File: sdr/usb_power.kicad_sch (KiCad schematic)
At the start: 9 parts, among them J1 USB_C_Receptacle_USB2.0, U1 AMS1117-3.3

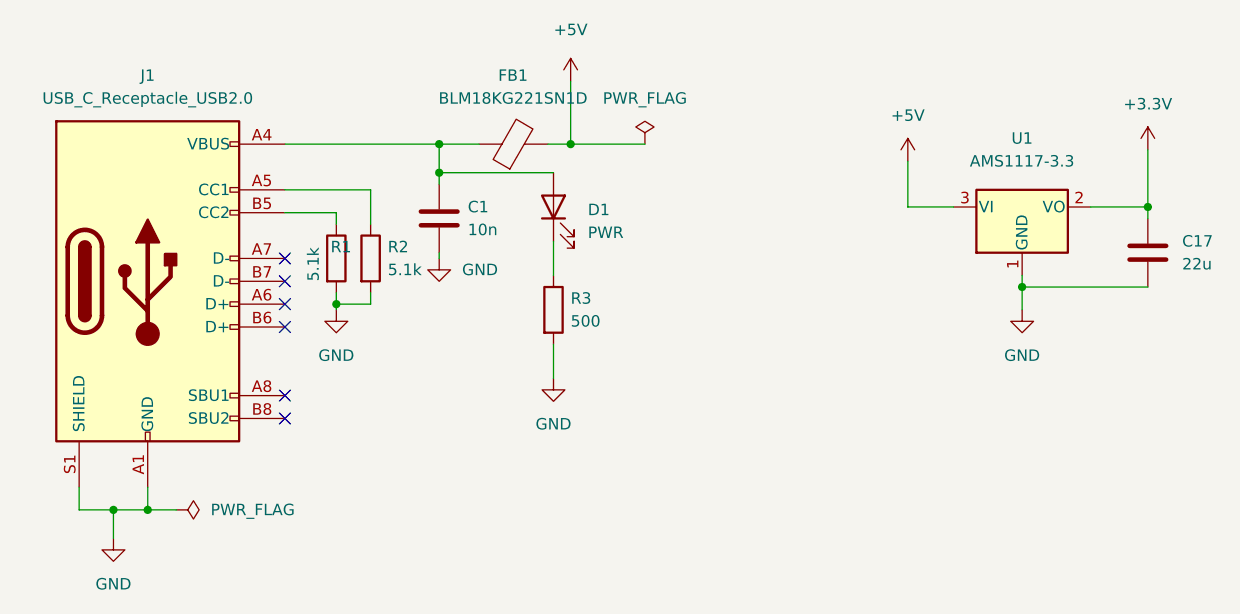
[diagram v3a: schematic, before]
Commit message: Tighten up design layout.
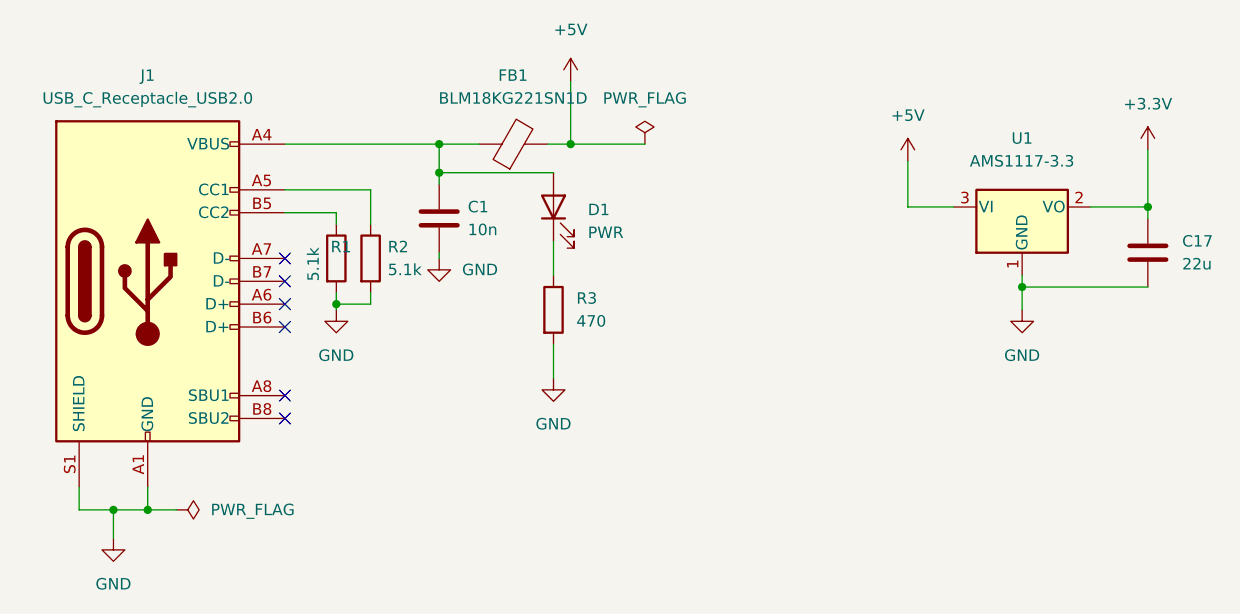
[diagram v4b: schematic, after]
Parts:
- C1: footprint Capacitor_SMD:C_0603_1608Metric -> Capacitor_SMD:C_0402_1005Metric
- R3: value 500 -> 470
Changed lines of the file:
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@@
   (symbol (lib_id "Device:R") (at 168.91 90.17 0) (unit 1)
     (in_bom yes) (on_board yes) (fields_autoplaced)
-    (property "Reference" "R3" (id 0) (at 170.815 88.8999 0)
-      (effects (font (size 1.27 1.27)) (justify left))
-    )
-    (property "Value" "500" (id 1) (at 170.815 91.4399 0)
+    (property "Reference" "R3" (id 0) (at 171.45 88.8999 0)
+      (effects (font (size 1.27 1.27)) (justify left))
+    )
+    (property "Value" "470" (id 1) (at 171.45 91.4399 0)
       (effects (font (size 1.27 1.27)) (justify left))
     )
@@
       (effects (font (size 1.27 1.27)) (justify left))
     )
-    (property "Footprint" "Capacitor_SMD:C_0603_1608Metric" (id 2) (at 157.1752 83.82 0)
-      (effects (font (size 1.27 1.27)) hide)
-    )
+    (property "Footprint" "Capacitor_SMD:C_0402_1005Metric" (id 2) (at 157.1752 83.82 0)
+      (effects (font (size 1.27 1.27)) hide)
+    )
